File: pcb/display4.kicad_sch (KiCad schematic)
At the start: 35 parts, among them Q37 2N7002K, Q38 2N7002K, Q39 2N7002K, Q40 2N7002K, Q41 BSS84, Q42 BSS84, Q43 BSS84, Q44 BSS84, Q45 BSS84, Q46 BSS84, Q47 BSS84, Q48 BSS84, U5 74HC595

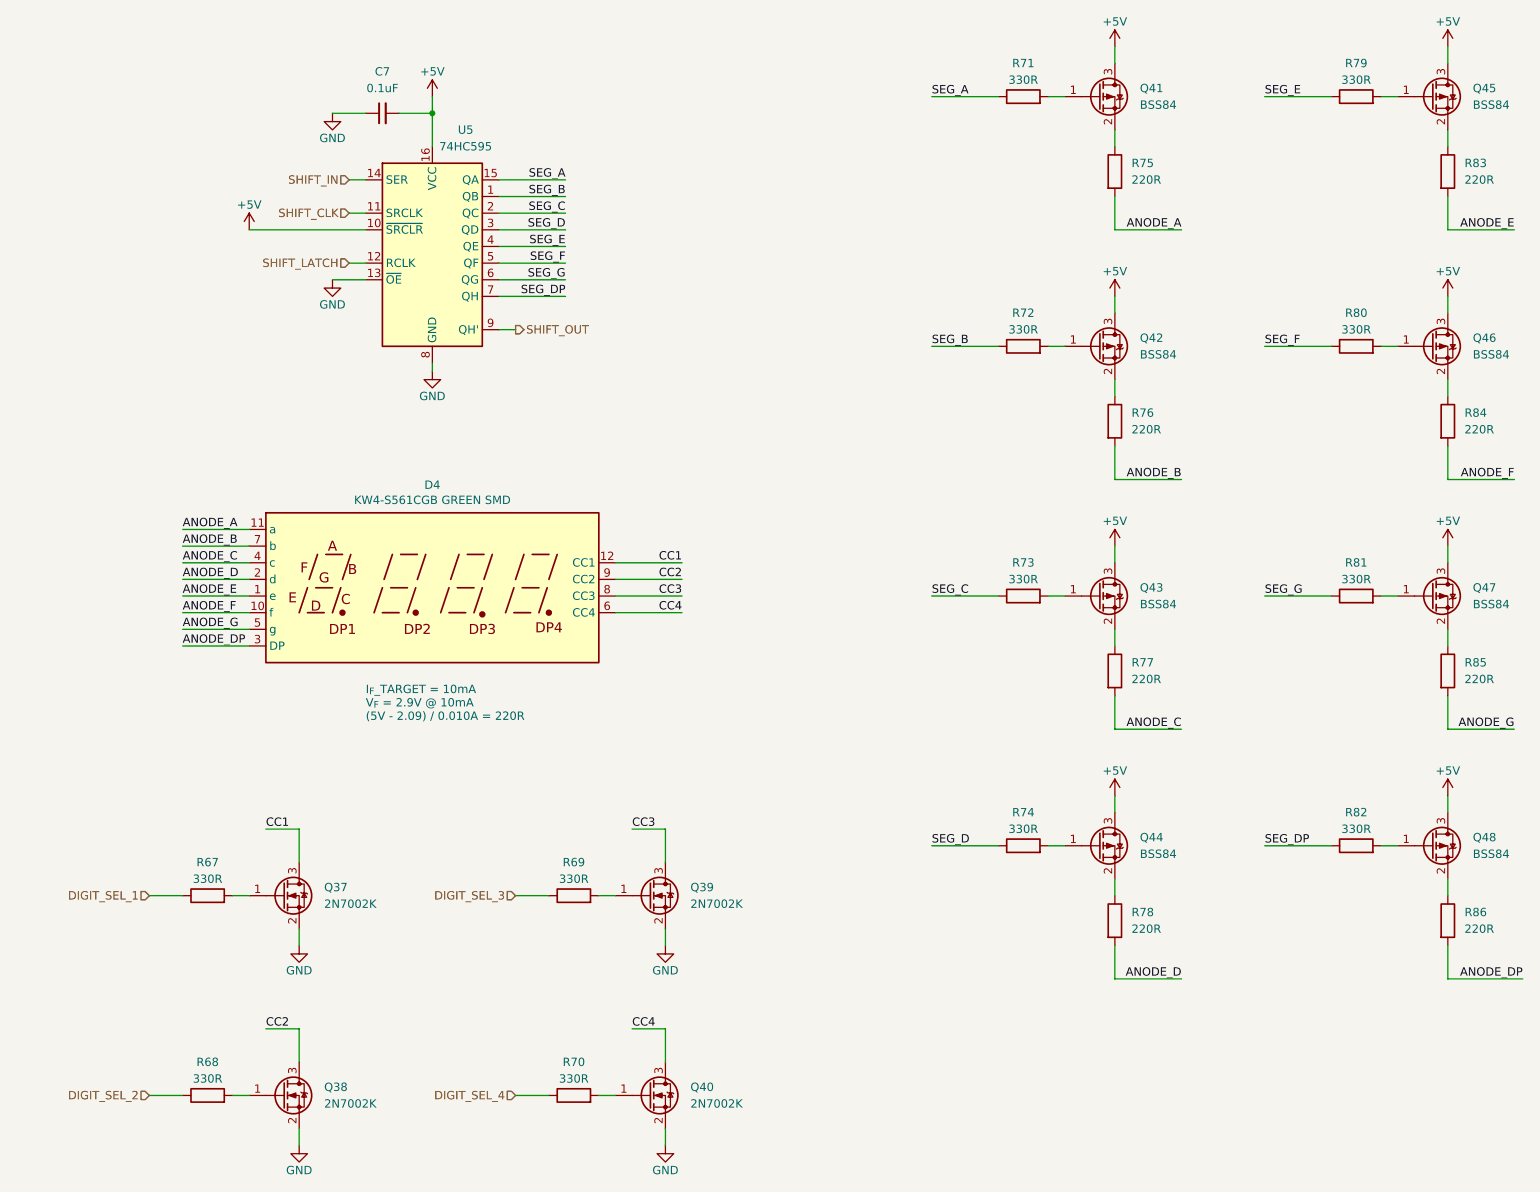
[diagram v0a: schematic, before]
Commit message: tentative schematic for common cathode
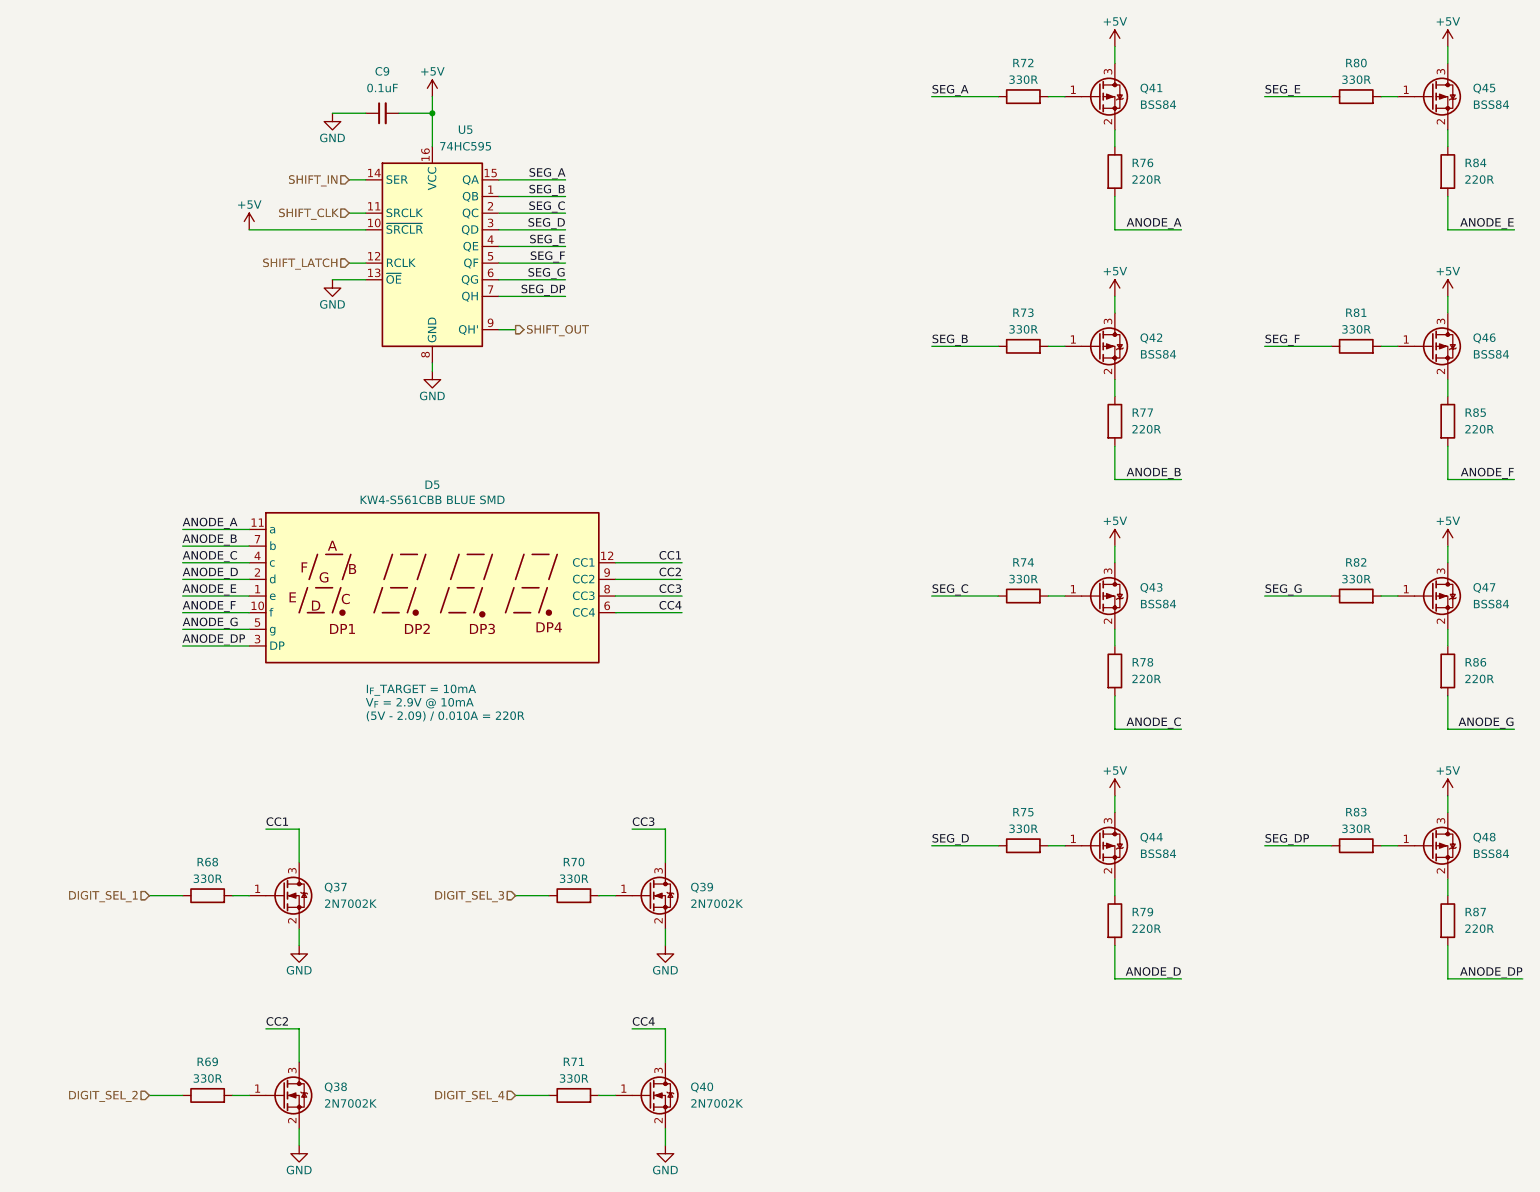
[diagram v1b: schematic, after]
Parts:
- C9: renamed from C7; footprint (none) -> Capacitor_SMD:C_0805_2012Metric_Pad1.18x1.45mm_HandSolder
- D5: renamed from D4; value KW4-S561CGB GREEN SMD -> KW4-S561CBB BLUE SMD
- R68: renamed from R67; footprint Resistor_SMD:R_0805_2012Metric_Pad1.15x1.40mm_HandSolder -> Resistor_SMD:R_0805_2012Metric_Pad1.20x1.40mm_HandSolder
- R69: renamed from R68; footprint Resistor_SMD:R_0805_2012Metric_Pad1.15x1.40mm_HandSolder -> Resistor_SMD:R_0805_2012Metric_Pad1.20x1.40mm_HandSolder
- R70: renamed from R69; footprint Resistor_SMD:R_0805_2012Metric_Pad1.15x1.40mm_HandSolder -> Resistor_SMD:R_0805_2012Metric_Pad1.20x1.40mm_HandSolder
- R71: renamed from R70; footprint Resistor_SMD:R_0805_2012Metric_Pad1.15x1.40mm_HandSolder -> Resistor_SMD:R_0805_2012Metric_Pad1.20x1.40mm_HandSolder
- R72: renamed from R71; footprint Resistor_SMD:R_0805_2012Metric_Pad1.15x1.40mm_HandSolder -> Resistor_SMD:R_0805_2012Metric_Pad1.20x1.40mm_HandSolder
- R73: renamed from R72; footprint Resistor_SMD:R_0805_2012Metric_Pad1.15x1.40mm_HandSolder -> Resistor_SMD:R_0805_2012Metric_Pad1.20x1.40mm_HandSolder
- R74: renamed from R73; footprint Resistor_SMD:R_0805_2012Metric_Pad1.15x1.40mm_HandSolder -> Resistor_SMD:R_0805_2012Metric_Pad1.20x1.40mm_HandSolder
- R75: renamed from R74; footprint Resistor_SMD:R_0805_2012Metric_Pad1.15x1.40mm_HandSolder -> Resistor_SMD:R_0805_2012Metric_Pad1.20x1.40mm_HandSolder
- R76: renamed from R75; footprint (none) -> Resistor_SMD:R_0805_2012Metric_Pad1.20x1.40mm_HandSolder
- R77: renamed from R76; footprint (none) -> Resistor_SMD:R_0805_2012Metric_Pad1.20x1.40mm_HandSolder
- R78: renamed from R77; footprint (none) -> Resistor_SMD:R_0805_2012Metric_Pad1.20x1.40mm_HandSolder
- R79: renamed from R78; footprint (none) -> Resistor_SMD:R_0805_2012Metric_Pad1.20x1.40mm_HandSolder
- R80: renamed from R79; footprint Resistor_SMD:R_0805_2012Metric_Pad1.15x1.40mm_HandSolder -> Resistor_SMD:R_0805_2012Metric_Pad1.20x1.40mm_HandSolder
- R81: renamed from R80; footprint Resistor_SMD:R_0805_2012Metric_Pad1.15x1.40mm_HandSolder -> Resistor_SMD:R_0805_2012Metric_Pad1.20x1.40mm_HandSolder
- R82: renamed from R81; footprint Resistor_SMD:R_0805_2012Metric_Pad1.15x1.40mm_HandSolder -> Resistor_SMD:R_0805_2012Metric_Pad1.20x1.40mm_HandSolder
- R83: renamed from R82; footprint Resistor_SMD:R_0805_2012Metric_Pad1.15x1.40mm_HandSolder -> Resistor_SMD:R_0805_2012Metric_Pad1.20x1.40mm_HandSolder
- R84: renamed from R83; footprint (none) -> Resistor_SMD:R_0805_2012Metric_Pad1.20x1.40mm_HandSolder
- R85: renamed from R84; footprint (none) -> Resistor_SMD:R_0805_2012Metric_Pad1.20x1.40mm_HandSolder
- R86: renamed from R85; footprint (none) -> Resistor_SMD:R_0805_2012Metric_Pad1.20x1.40mm_HandSolder
- R87: renamed from R86; footprint (none) -> Resistor_SMD:R_0805_2012Metric_Pad1.20x1.40mm_HandSolder

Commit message: common anode schematic
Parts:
- removed C9: 0.1uF, Capacitor_SMD:C_0805_2012Metric_Pad1.18x1.45mm_HandSolder, symbol Device:C_Small
- removed D5: KW4-S561CBB BLUE SMD, mtg_life_counter:KW4-S561xxB_SMD, symbol mtg_life_counter:KW4-S561CxB
- removed Q37, Q38, Q39, Q40: 2N7002K, Package_TO_SOT_SMD:SOT-23, symbol Transistor_FET:2N7002K
- removed Q41, Q42, Q43, Q44, Q45, Q46, Q47, Q48: BSS84, Package_TO_SOT_SMD:SOT-23, symbol Transistor_FET:BSS84
- removed R68, R69, R70, R71, R72, R73, R74, R75, R80, R81, R82, R83: 330R, Resistor_SMD:R_0805_2012Metric_Pad1.20x1.40mm_HandSolder, symbol Device:R
- removed R76, R77, R78, R79, R84, R85, R86, R87: 220R, Resistor_SMD:R_0805_2012Metric_Pad1.20x1.40mm_HandSolder, symbol Device:R
- removed U5: 74HC595, Package_SO:SOIC-16_3.9x9.9mm_P1.27mm, symbol 74xx:74HC595
- added D5: KW4-S561ABB, mtg_life_counter:KW4-S561xxB_SMD, symbol mtg_life_counter:KW4-S561AxB
- added Q13, Q14, Q15, Q16: DMG2301L, Package_TO_SOT_SMD:SOT-23, symbol Transistor_FET:DMG2301L
- added R47, R48, R49, R50: 330R, Resistor_SMD:R_0805_2012Metric_Pad1.20x1.40mm_HandSolder, symbol Device:R
- added R51, R52, R53, R54, R55, R56, R57, R58: 220R, Resistor_SMD:R_0805_2012Metric_Pad1.20x1.40mm_HandSolder, symbol Device:R
- added R59: 10k, Resistor_SMD:R_0805_2012Metric_Pad1.20x1.40mm_HandSolder, symbol Device:R
- added U5: TPIC6C596, Package_SO:SOIC-16_3.9x9.9mm_P1.27mm, symbol mtg_life_counter:TPIC6C596
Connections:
- net +5V: now also Q13.3 (D), Q14.3 (D), Q15.3 (D), Q16.3 (D), R59.1, U5.1 (VCC)
- net DIGIT_SEL_1: now also R47.1
- net DIGIT_SEL_2: now also R48.1
- net DIGIT_SEL_3: now also R49.1
- net DIGIT_SEL_4: now also R50.1
- net GND: now also U5.16 (GND), U5.8 (~{G})
- net SHIFT_CLK: now also U5.15 (SRCK)
- net SHIFT_IN: now also U5.2 (SER_IN)
- net SHIFT_LATCH: now also U5.10 (RCLK)
- net SHIFT_OUT: now also U5.9 (SER_OUT)
- new net: Q13.1 (G), R47.2
- new net: Q14.1 (G), R48.2
- new net: R59.2, U5.7 (~{SRCLR})
- new net: Q16.1 (G), R50.2
- new net: Q15.1 (G), R49.2
- new net AA: D5.11 (a), R51.1
- new net AB: D5.7 (b), R52.1
- new net AC: D5.4 (c), R53.1
- new net AD: D5.2 (d), R54.1
- new net ADP: D5.3 (DP), R58.1
- new net AE: D5.1 (e), R55.1
- new net AF: D5.10 (f), R56.1
- new net AG: D5.5 (g), R57.1
- new net CA1: D5.12 (CA1), Q13.2 (S)
- new net CA2: D5.9 (CA2), Q14.2 (S)
- new net CA3: D5.8 (CA3), Q15.2 (S)
- new net CA4: D5.6 (CA4), Q16.2 (S)
- new net SA: R51.2, U5.3 (DRAIN0)
- new net SB: R52.2, U5.4 (DRAIN1)
- new net SC: R53.2, U5.5 (DRAIN2)
- new net SD: R54.2, U5.6 (DRAIN3)
- new net SDP: R58.2, U5.14 (DRAIN7)
- new net SE: R55.2, U5.11 (DRAIN4)
- new net SF: R56.2, U5.12 (DRAIN5)
- new net SG: R57.2, U5.13 (DRAIN6)
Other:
- note added: "I_{F}_TARGET = 10mA V_{F} = 2.9V @ 10mA (5V - 2.9) / 0.010A = 220R"
- note removed: "I_{F}_TARGET = 10mA V_{F} = 2.9V @ 10mA (5V - 2.09) / 0.010A = 220R"

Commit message: continue wip
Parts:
- added C9: 0.1uF, Capacitor_SMD:C_0805_2012Metric_Pad1.18x1.45mm_HandSolder, symbol Device:C_Small
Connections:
- net +5V: now also C9.1
- net GND: now also C9.2
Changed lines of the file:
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@@
+	(wire
+		(pts
+			(xy 200.66 50.8) (xy 200.66 53.34)
+		)
+		(stroke
+			(width 0)
+			(type default)
+		)
+	)
 	(wire
 		(pts
@@
 		(pts
 			(xy 93.98 86.36) (xy 93.98 134.62)
+		)
+		(stroke
+			(width 0)
+			(type default)
+		)
+	)
+	(wire
+		(pts
+			(xy 200.66 58.42) (xy 200.66 60.96)
 		)
 		(stroke
@@
 				(path "/1883df74-0bd5-446c-9076-f848bb3cfebf/0915e7ce-f0a0-446b-99c3-b1ae0eab9275"
 					(reference "Q14")
+					(unit 1)
+				)
+			)
+		)
+	)
+	(symbol
+		(lib_id "Device:C_Small")
+		(at 200.66 55.88 0)
+		(unit 1)
+		(exclude_from_sim no)
+		(in_bom yes)
+		(on_board yes)
+		(dnp no)
+		(property "Reference" "C9"
+			(at 198.12 54.6162 0)
+			(effects
+				(font
+					(size 1.27 1.27)
+				)
+				(justify right)
+			)
+		)
+		(property "Value" "0.1uF"
+			(at 198.12 57.1562 0)
+			(effects
+				(font
+					(size 1.27 1.27)
+				)
+				(justify right)
+			)
+		)
+		(property "Footprint" "Capacitor_SMD:C_0805_2012Metric_Pad1.18x1.45mm_HandSolder"
+			(at 200.66 55.88 0)
+			(effects
+				(font
+					(size 1.27 1.27)
+				)
+				(hide yes)
+			)
+		)
+		(property "Datasheet" "~"
+			(at 200.66 55.88 0)
+			(effects
+				(font
+					(size 1.27 1.27)
+				)
+				(hide yes)
+			)
+		)
+		(property "Description" "Unpolarized capacitor, small symbol"
+			(at 200.66 55.88 0)
+			(effects
+				(font
+					(size 1.27 1.27)
+				)
+				(hide yes)
+			)
+		)
+		(pin "2"
+		)
+		(pin "1"
+		)
+		(instances
+			(project "mtg_life_counter"
+				(path "/1883df74-0bd5-446c-9076-f848bb3cfebf/0915e7ce-f0a0-446b-99c3-b1ae0eab9275"
+					(reference "C9")
 					(unit 1)
 				)
@@
 	)
 	(symbol
+		(lib_id "power:+5V")
+		(at 200.66 50.8 0)
+		(unit 1)
+		(exclude_from_sim no)
+		(in_bom yes)
+		(on_board yes)
+		(dnp no)
+		(property "Reference" "#PWR069"
+			(at 200.66 54.61 0)
+			(effects
+				(font
+					(size 1.27 1.27)
+				)
+				(hide yes)
+			)
+		)
+		(property "Value" "+5V"
+			(at 200.66 46.99 0)
+			(effects
+				(font
+					(size 1.27 1.27)
+				)
+			)
+		)
+		(property "Footprint" ""
+			(at 200.66 50.8 0)
+			(effects
+				(font
+					(size 1.27 1.27)
+				)
+				(hide yes)
+			)
+		)
+		(property "Datasheet" ""
+			(at 200.66 50.8 0)
+			(effects
+				(font
+					(size 1.27 1.27)
+				)
+				(hide yes)
+			)
+		)
+		(property "Description" "Power symbol creates a global label with name \"+5V\""
+			(at 200.66 50.8 0)
+			(effects
+				(font
+					(size 1.27 1.27)
+				)
+				(hide yes)
+			)
+		)
+		(pin "1"
+		)
+		(instances
+			(project "mtg_life_counter"
+				(path "/1883df74-0bd5-446c-9076-f848bb3cfebf/0915e7ce-f0a0-446b-99c3-b1ae0eab9275"
+					(reference "#PWR069")
+					(unit 1)
+				)
+			)
+		)
+	)
+	(symbol
 		(lib_id "Device:R")
 		(at 49.53 124.46 90)
@@
 					(unit 1)
 				)
+			)
+		)
+	)
+	(symbol
+		(lib_id "power:GND")
+		(at 200.66 60.96 0)
+		(unit 1)
+		(exclude_from_sim no)
+		(in_bom yes)
+		(on_board yes)
+		(dnp no)
+		(property "Reference" "#PWR070"
+			(at 200.66 67.31 0)
+			(effects
+				(font
+					(size 1.27 1.27)
+				)
+				(hide yes)
+			)
+		)
+		(property "Value" "GND"
+			(at 200.66 64.77 0)
+			(effects
+				(font
+					(size 1.27 1.27)
+				)
+			)
+		)
+		(property "Footprint" ""
+			(at 200.66 60.96 0)
+			(effects
+				(font
+					(size 1.27 1.27)
+				)
+				(hide yes)
+			)
+		)
+		(property "Datasheet" ""
+			(at 200.66 60.96 0)
+			(effects
+				(font
+					(size 1.27 1.27)
+				)
+				(hide yes)
+			)
+		)
+		(property "Description" "Power symbol creates a global label with name \"GND\" , ground"
+			(at 200.66 60.96 0)
+			(effects
+				(font
+					(size 1.27 1.27)
+				)
+				(hide yes)
+			)
+		)
+		(pin "1"
+		)
+		(instances
+			(project "mtg_life_counter"
+				(path "/1883df74-0bd5-446c-9076-f848bb3cfebf/0915e7ce-f0a0-446b-99c3-b1ae0eab9275"
+					(reference "#PWR070")
+					(unit 1)
+				)
